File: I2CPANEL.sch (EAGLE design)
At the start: 47 parts, among them IC1 ATMEGA32U4-QFN

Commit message: Schematic and routing for v1.0 release
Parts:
- removed C1: 100nF 0603, freetronics-master-v1.1:CAP0603
- removed C3, C4: 1uF 0603, freetronics-master-v1.1:CAP0603
- removed C5, C6: 15pF 0603, freetronics-master-v1.1:CAP0603
- removed F1: 500mA PTC 1812, rcl:L-EUL1812
- removed IC1: ATMEGA32U4-QFN, freetronics-jon:ATMEGA32U4-QFN
- removed ICSP: ICSP, pinhead:PINHD-2X3
- removed LED2: RED, freetronics-jon:LED0603
- removed LED3: GREEN, freetronics-jon:LED0603
- removed R1, R6: 22R, freetronics-jon:RESISTOR0603
- removed R18: 5.1K, freetronics-original:RESISTOR0603
- removed R2: 10K 0603, freetronics-master-v1.1:RESISTOR0603
- removed R4, R5: 1K, freetronics-jon:RESISTOR0603
- removed S10: 10, freetronics-original:TAC_SWITCHPTH
- removed S11: 11, freetronics-original:TAC_SWITCHPTH
- removed S12: 12, freetronics-original:TAC_SWITCHPTH
- removed S13: 13, freetronics-original:TAC_SWITCHPTH
- removed S14: 14, freetronics-original:TAC_SWITCHPTH
- removed S15: 15, freetronics-original:TAC_SWITCHPTH
- removed S16: 16, freetronics-original:TAC_SWITCHPTH
- removed S17: 17, freetronics-original:TAC_SWITCHPTH
- removed S18: 18, freetronics-original:TAC_SWITCHPTH
- removed S19: 19, freetronics-original:TAC_SWITCHPTH
- removed S20: 20, freetronics-original:TAC_SWITCHPTH
- removed S21: RESET, freetronics-jon:TAC_SWITCH_2PINSMT
- removed S22: HWB, freetronics-jon:TAC_SWITCH_2PINSMT
- removed S7: 7, freetronics-original:TAC_SWITCHPTH
- removed S8: 8, freetronics-original:TAC_SWITCHPTH
- removed S9: 9, freetronics-original:TAC_SWITCHPTH
- removed U$15: USB-C, freetronics-jon:USB-C
- removed XTL1: 16MHz, freetronics-jon:CRYSTAL-GND3X2
- removed Z1, Z2: PGB1010603, freetronics-master-v1.1:RESISTOR0603
- added IC2: MCP23017SO, microchip:MCP23017SO
- added JP1: M100.1, freetronics-original:M100.1
- added JP3: OLED, freetronics-jon:M04PTH
- added R27, R28: 4K7, freetronics-master-v1:RESISTOR0603
- added R29, R30, R31: 10K, freetronics-master-v1:RESISTOR0603
- added SJ2, SJ3, SJ4, SJ5: (no value), freetronics-jon:SJN
- C2: value 100nF 0603 -> 1uF
- SJ1: value HWB -> (none)
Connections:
- removed net 3V3: C4.2, IC1.UCAP
- removed net 5V: C2.1, C3.1, F1.2, IC1.AVCC, IC1.AVCC1, IC1.UVCC, IC1.VBUS, IC1.VCC, IC1.VCC1, ICSP.2, JP2.3, R2.2, R3.2, R4.2, R5.2
- removed net A0: IC1.PF7(ADC7(TDI)
- removed net A1: IC1.PF6(ADC6/TDO)
- removed net A2: IC1.PF5(ADC5/TMS)
- removed net A3: IC1.PF4(ADC4/TCK)
- removed net A4: IC1.PF1(ADC1)
- removed net A5: IC1.PF0(ADC0)
- removed net AREF: C1.1, IC1.AREF
- removed net COL0: IC1.PD4(ICP1/ADC8), S1.1, S1.2, S13.1, S13.2, S17.1, S17.2, S5.1, S5.2, S9.1, S9.2
- removed net COL1: IC1.PC6(OC3A/!OC4A!), S10.1, S10.2, S14.1, S14.2, S18.1, S18.2, S2.1, S2.2, S6.1, S6.2
- removed net COL2: IC1.PD2(INT2/RXD1), S11.1, S11.2, S15.1, S15.2, S19.1, S19.2, S3.1, S3.2, S7.1, S7.2
- removed net COL3: IC1.PD3(INT3/TXD1), S12.1, S12.2, S16.1, S16.2, S20.1, S20.2, S4.1, S4.2, S8.1, S8.2
- removed net D+: R6.1, U$15.D+@A6, U$15.D+@B6, Z2.2
- removed net D-: R1.1, U$15.D-@A7, U$15.D-@B7, Z1.2
- removed net D11: IC1.PB7(OC0A/OC1C/RTS)
- removed net D13: IC1.PC7(ICP3/CLK0/OC4A)
- removed net D2_SDA: IC1.PD1(INT1/SDA), JP2.1
- removed net D3_SCL: IC1.PD0(INT0/OC0B/SCL), JP2.2
- removed net D7_AIN0: IC1.PE6
- removed net HWB: IC1.PE2(HWB), S22.P, SJ1.1
- removed net MISO: IC1.PB3(PDO/MISO), ICSP.1
- removed net MOSI: IC1.PB2(PDI/MOSI), ICSP.4
- removed net N$11: C5.2, IC1.XTAL1, XTL1.XTL2
- removed net N$12: C6.2, IC1.XTAL2, XTL1.XTL1
- removed net N$67: R18.2, U$15.CC1, U$15.CC2
- removed net RD+: IC1.D+, R6.2
- removed net RD-: IC1.D-, R1.2
- removed net RESET: IC1./RESET, ICSP.5, R2.1, S21.S
- removed net ROW0: IC1.PD7(OC4D/ADC10/T0), S1.3, S1.4, S2.3, S2.4, S3.3, S3.4, S4.3, S4.4
- removed net ROW1: IC1.PD6(T1/OC4D/ADC9), S5.3, S5.4, S6.3, S6.4, S7.3, S7.4, S8.3, S8.4
- removed net ROW2: IC1.PB4(ADC11), S10.3, S10.4, S11.3, S11.4, S12.3, S12.4, S9.3, S9.4
- removed net ROW3: IC1.PB5(OC1A/!OC4B!/ADC12), S13.3, S13.4, S14.3, S14.4, S15.3, S15.4, S16.3, S16.4
- removed net ROW4: IC1.PB6(OC1B/!OC4B!/ADC13), S17.3, S17.4, S18.3, S18.4, S19.3, S19.4, S20.3, S20.4
- removed net RXLED_SS: IC1.PB0(SS), LED3.C
- removed net SCK: IC1.PB1(SCK), ICSP.3
- removed net TX_LED: IC1.PD5(XCK/CTS), LED2.C
- removed net USB+: F1.1, U$15.V+@A4, U$15.V+@A9, U$15.V+@B4, U$15.V+@B9
- new net ADDR0: IC2.A0, R29.2, SJ1.1
- new net ADDR1: IC2.A1, R30.2, SJ2.1
- new net ADDR2: IC2.A2, R31.2, SJ3.1
- new net GPA1: IC2.GPA1, S1.1, S1.2
- new net GPA2: IC2.GPA2, S2.1, S2.2
- new net GPA3: IC2.GPA3, S3.1, S3.2
- new net GPA4: IC2.GPA4, S4.1, S4.2
- new net GPA5: IC2.GPA5, S5.1, S5.2
- new net GPA6: IC2.GPA6, S6.1, S6.2
- new net N$1: IC2.GPB0, JP1.1
- new net N$2: IC2.GPB1, JP1.2
- new net N$3: IC2.GPB2, JP1.3
- new net N$4: IC2.GPB3, JP1.4
- new net N$42: R27.2, SJ4.1
- new net N$43: R28.2, SJ5.1
- new net N$5: IC2.GPB4, JP1.5
- new net N$9: IC2.GPB7, JP1.8
- new net SCL: IC2.SCL, JP2.2, JP3.2, R27.1
- new net SDA: IC2.SDA, JP2.1, JP3.1, R28.1
- new net VCC: C2.1, IC2.!RESET, IC2.VDD, JP1.9, JP2.3, JP3.3, R3.2, SJ1.2, SJ2.2, SJ3.2, SJ4.2, SJ5.2
- net GND: now also IC2.VSS, JP1.10, JP3.4, R29.1, R30.1, R31.1, S1.3, S1.4, S2.3, S2.4, S3.3, S3.4, S4.3, S4.4, S5.3, S5.4, S6.3, S6.4; no longer C1.2, C3.2, C4.1, C5.1, C6.1, IC1.GND, IC1.GND1, IC1.GND2, IC1.GND3, IC1.TGND, IC1.UGND, ICSP.6, R18.1, S21.P, S22.S, SJ1.2, U$15.GND@A1, U$15.GND@A12, U$15.GND@B1, U$15.GND@B12, U$15.GND@CASE1, U$15.GND@CASE2, U$15.GND@CASE3, U$15.GND@CASE4, U$15.GND@FIX1, U$15.GND@FIX2, U$15.GND@FIX3, U$15.GND@FIX4, XTL1.GND, XTL1.GND2, Z1.1, Z2.1
- net N$7: now also IC2.GPB5, JP1.6; no longer LED2.A, R4.1
- net N$8: now also IC2.GPB6, JP1.7; no longer LED3.A, R5.1
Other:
- note added: "(C)2019 SuperHouse Automation Pty Ltd: www.superhouse.tv"
- note added: "1"
- note added: "2"
- note added: "4"
- note added: "Buttons"
- note added: "I2C Header"
- note added: "I2C I/O Expander"
- note added: "Possible future features: * LED connected to spare GPIO * Piezo connected to spare GPIO * Other I2C sensors such as temperature https://raspi.tv/2013/using-the-mcp23017-port-expander-with-wiringpi2-to-give-you-16-new-gpio-ports-part-3"
- note added: "SKU: I2CPANEL"
- note added: "Spare GPIOs GPB0 - GPB7"
- note added: "SuperHouse I2C Control Panel"
- note added: "V1.0 (2019-05-22)"
- note added: "www.superhouse.tv/i2cpanel"
- note removed: "(C)2018 SuperHouse Automation Pty Ltd: www.superhouse.tv"
- note removed: "ATmega32u4 MCU"
- note removed: "Col0: D4 Col1: D5 Col2: D0 Col3: D1 Row0: D6 Row1: D12 Row2: D8 Row3: D9 Row4: D10"
- note removed: "D0"
- note removed: "D1"
- note removed: "D10"
- note removed: "D10_A11"
- note removed: "D12"
- note removed: "D4"
- note removed: "D4_A6"
- note removed: "D5"
- note removed: "D6"
- note removed: "D6_A8"
- note removed: "D8"
- note removed: "D8_A9"
- note removed: "D9"
- note removed: "D9_A10"
- note removed: "HWB button & solder jumper: HWB should be shorted normally to enable the bootloader, and removed to disable the bootloader and jump straight to the program. However, the official Leonardo bootloader fuse settings don't enable the HWB pin. Use custom fuse settings to allow the keypad to boot straight to keypad mode without this jumper in place, or go to the bootloader with the jumper."
- note removed: "ICSP Header"
- note removed: "Keypad Matrix"
- note removed: "SKU: LPMINI"
- note removed: "SuperHouse LeoPad Mini"
- note removed: "V1.0 (2018-06-13)"
- note removed: "www.superhouse.tv/lpmini"
- moved on the sheet: C2, JP2, LED1, R3, S1, S2, S3, S4, S5, S6, SJ1

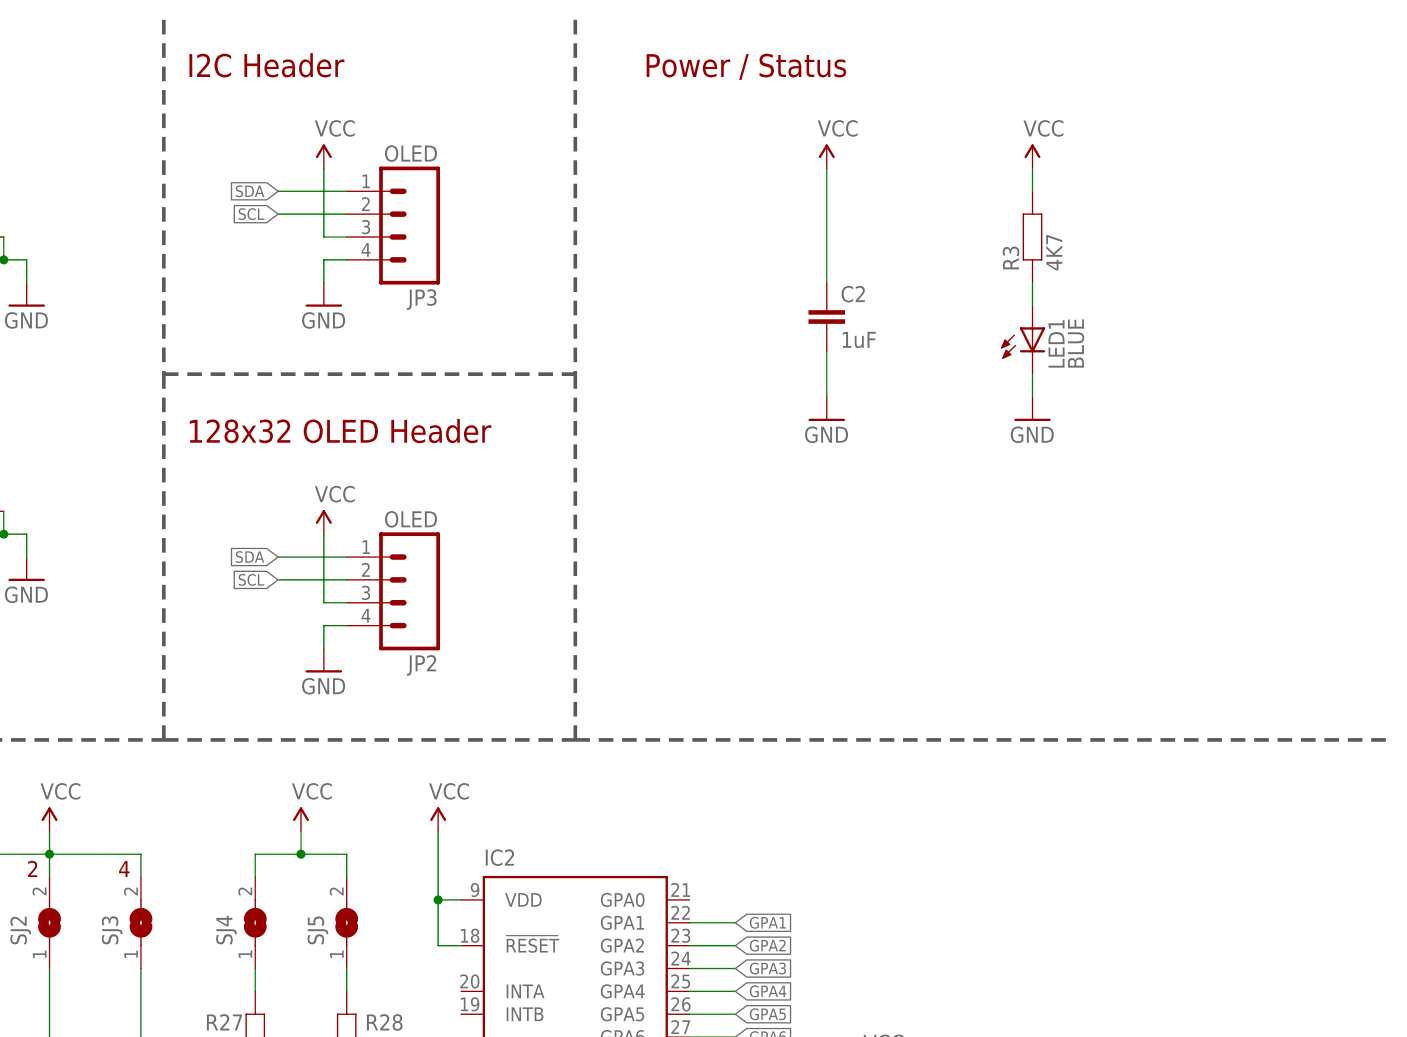
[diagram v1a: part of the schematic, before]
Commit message: Major rework to use 128x32 screen for v1.0 release
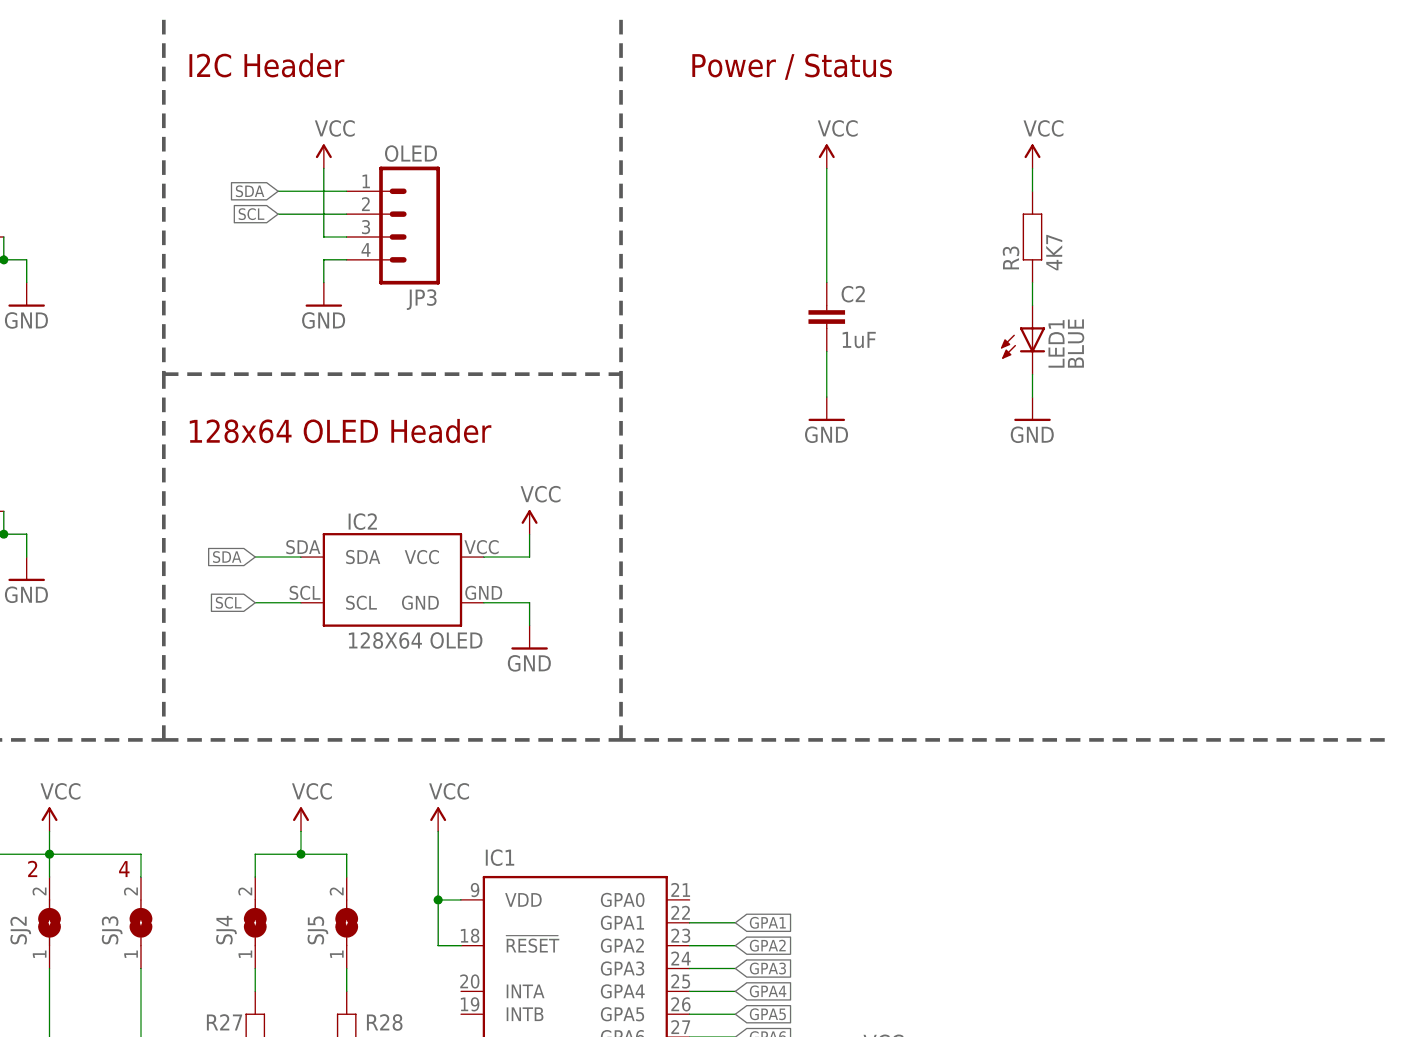
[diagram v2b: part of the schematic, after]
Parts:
- removed JP2: OLED, freetronics-jon:M04PTH
- added IC1: MCP23017SO, microchip:MCP23017SO
- IC2: value MCP23017SO -> 128X64 OLED; device microchip:MCP23017SO -> freetronics-jon:OLED-I2C128X32
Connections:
- net ADDR0: now also IC1.A0; no longer IC2.A0
- net ADDR1: now also IC1.A1; no longer IC2.A1
- net ADDR2: now also IC1.A2; no longer IC2.A2
- net GND: now also IC1.VSS, IC2.GND; no longer IC2.VSS, JP2.4
- net GPA1: now also IC1.GPA1; no longer IC2.GPA1
- net GPA2: now also IC1.GPA2; no longer IC2.GPA2
- net GPA3: now also IC1.GPA3; no longer IC2.GPA3
- net GPA4: now also IC1.GPA4; no longer IC2.GPA4
- net GPA5: now also IC1.GPA5; no longer IC2.GPA5
- net GPA6: now also IC1.GPA6; no longer IC2.GPA6
- net N$1: now also IC1.GPB0; no longer IC2.GPB0
- net N$2: now also IC1.GPB1; no longer IC2.GPB1
- net N$3: now also IC1.GPB2; no longer IC2.GPB2
- net N$4: now also IC1.GPB3; no longer IC2.GPB3
- net N$5: now also IC1.GPB4; no longer IC2.GPB4
- net N$7: now also IC1.GPB5; no longer IC2.GPB5
- net N$8: now also IC1.GPB6; no longer IC2.GPB6
- net N$9: now also IC1.GPB7; no longer IC2.GPB7
- net SCL: now also IC1.SCL; no longer JP2.2
- net SDA: now also IC1.SDA; no longer JP2.1
- net VCC: now also IC1.!RESET, IC1.VDD, IC2.VCC; no longer IC2.!RESET, IC2.VDD, JP2.3
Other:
- note added: "128x64 OLED Header"
- note removed: "128x32 OLED Header"

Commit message: Added mechanical dimensions
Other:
- note added: "Possible future features: * LED connected to spare GPIO * Piezo connected to spare GPIO * Other I2C sensors such as temperature * Illuminated tact buttons https://raspi.tv/2013/using-the-mcp23017-port-expander-with-wiringpi2-to-give-you-16-new-gpio-ports-part-3"
- note removed: "Possible future features: * LED connected to spare GPIO * Piezo connected to spare GPIO * Other I2C sensors such as temperature https://raspi.tv/2013/using-the-mcp23017-port-expander-with-wiringpi2-to-give-you-16-new-gpio-ports-part-3"
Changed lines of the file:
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@@
  * Piezo connected to spare GPIO
  * Other I2C sensors such as temperature
+ * Illuminated tact buttons
 https://raspi.tv/2013/using-the-mcp23017-port-expander-with-wiringpi2-to-give-you-16-new-gpio-ports-part-3</text>
 <text x="10.16" y="93.98" size="2.54" layer="94" ratio="12">I2C I/O Expander</text>

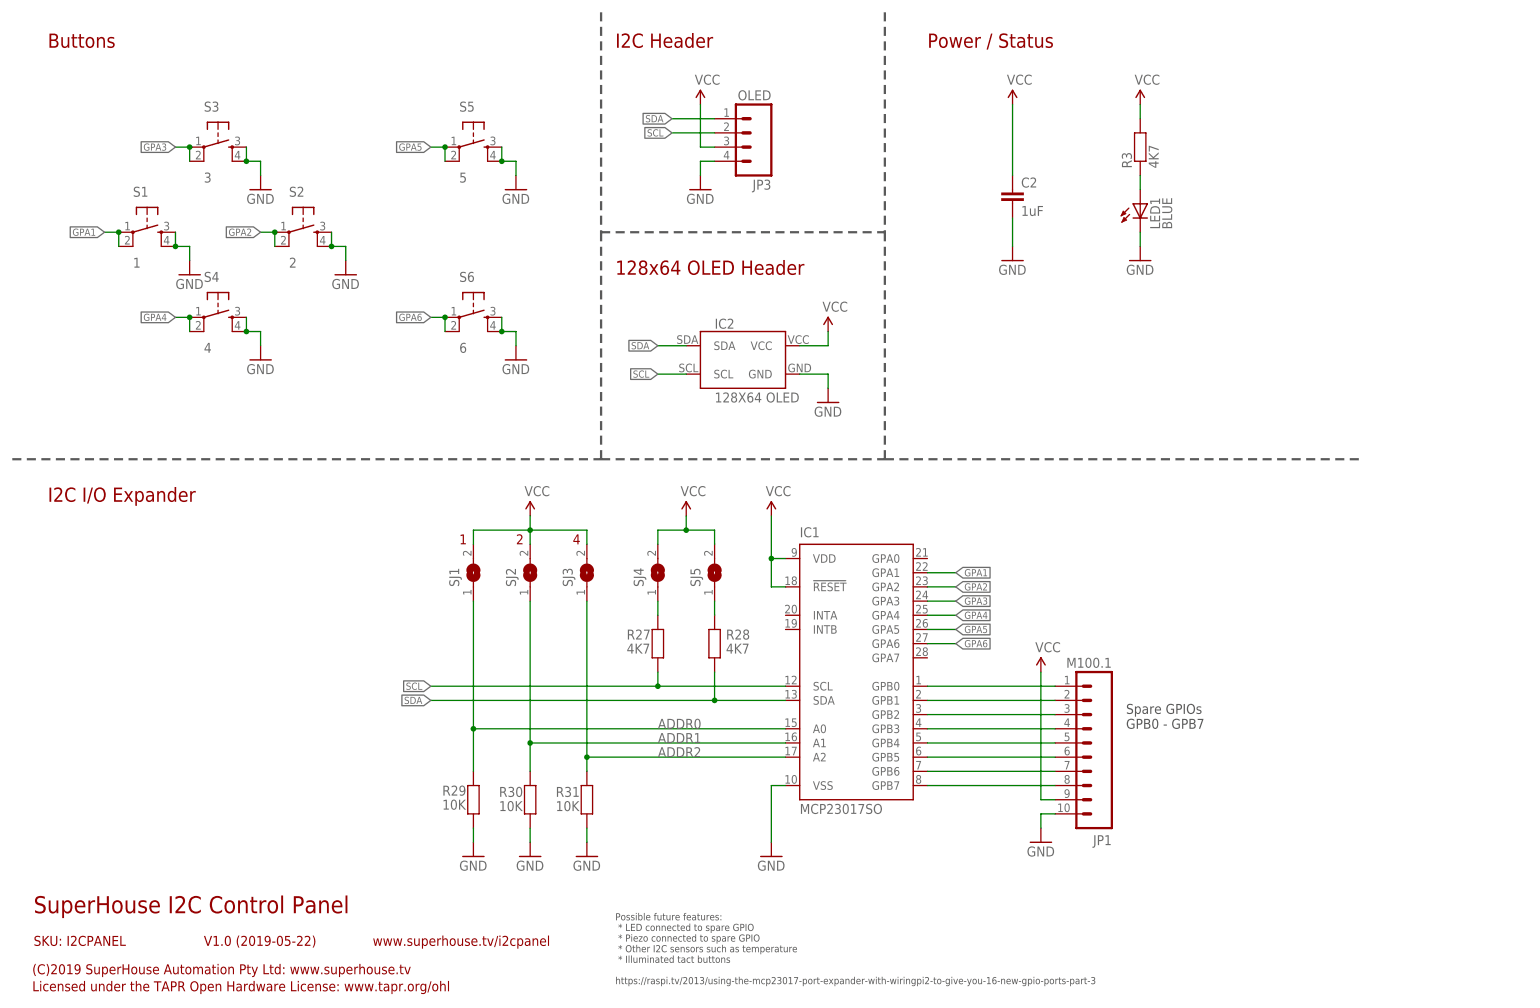
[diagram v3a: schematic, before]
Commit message: Added second OLED mount
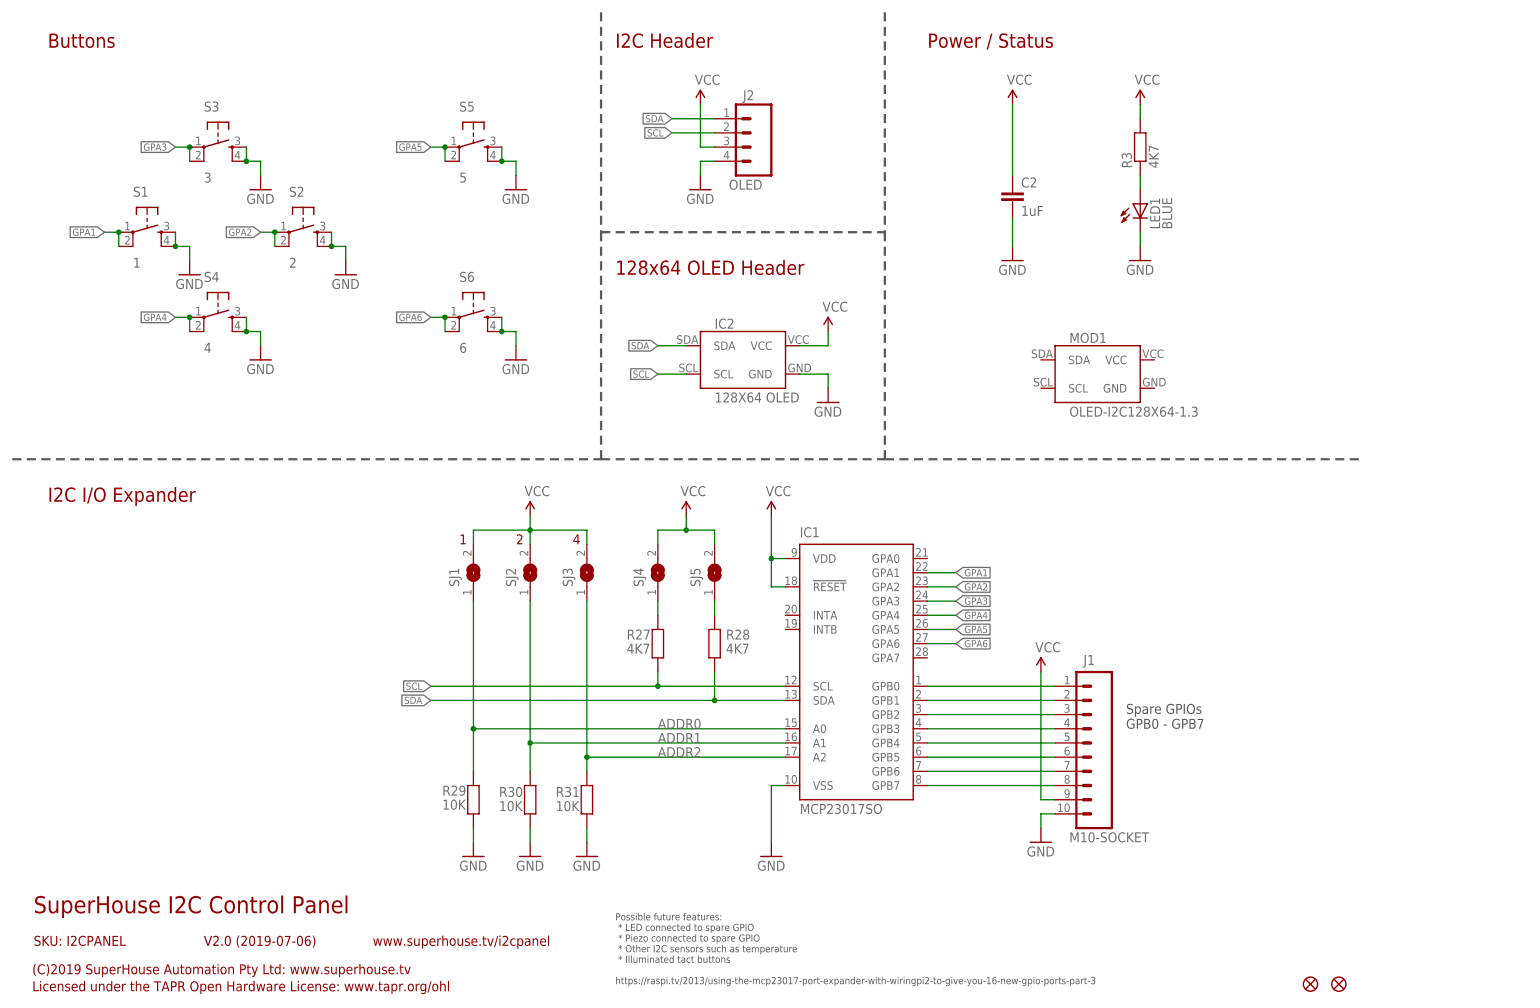
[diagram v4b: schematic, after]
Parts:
- removed JP1: M100.1, freetronics-original:M100.1
- removed JP3: OLED, freetronics-jon:M04PTH
- added FID1, FID2: FIDUCIAL1X2.5, freetronics:FIDUCIAL1X2.5
- added J1: M10-SOCKET, SuperHouse-Connectors:M10-SOCKET
- added J2: OLED, SuperHouse-Connectors:M04-PIN
- added MOD1: OLED-I2C128X64-1.3, SuperHouse-Displays:OLED-I2C128X64-1.3
- C2: device freetronics-master-v1.1:CAP0603 -> SuperHouse-DiscreteSemi:CAP0603
- IC1: device microchip:MCP23017SO -> SuperHouse-ICs:MCP23017SO
- LED1: device freetronics-jon:LED0603 -> SuperHouse-LEDs:LED0603
- R27, R28, R29, R30, R31: device freetronics-master-v1:RESISTOR0603 -> SuperHouse-DiscreteSemi:RESISTOR0603
- R3: device freetronics-jon:RESISTOR0603 -> SuperHouse-DiscreteSemi:RESISTOR0603
- S1, S2, S3, S4, S5, S6: device freetronics-original:TAC_SWITCHPTH -> SuperHouse-Switches:TAC_SWITCH-PTH-6
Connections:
- net GND: now also J1.10, J2.4; no longer JP1.10, JP3.4
- net N$1: now also J1.1; no longer JP1.1
- net N$2: now also J1.2; no longer JP1.2
- net N$3: now also J1.3; no longer JP1.3
- net N$4: now also J1.4; no longer JP1.4
- net N$5: now also J1.5; no longer JP1.5
- net N$7: now also J1.6; no longer JP1.6
- net N$8: now also J1.7; no longer JP1.7
- net N$9: now also J1.8; no longer JP1.8
- net SCL: now also J2.2; no longer JP3.2
- net SDA: now also J2.1; no longer JP3.1
- net VCC: now also J1.9, J2.3; no longer JP1.9, JP3.3
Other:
- note added: "V2.0 (2019-07-06)"
- note removed: "V1.0 (2019-05-22)"
